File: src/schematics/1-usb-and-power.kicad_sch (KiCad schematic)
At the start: 49 parts, among them Q101 NX6008NBKW, U101 MP5016HGQH, U102 BQ24392RSER, U103 FUSB302BMPX, U104 TPS628512DRLR

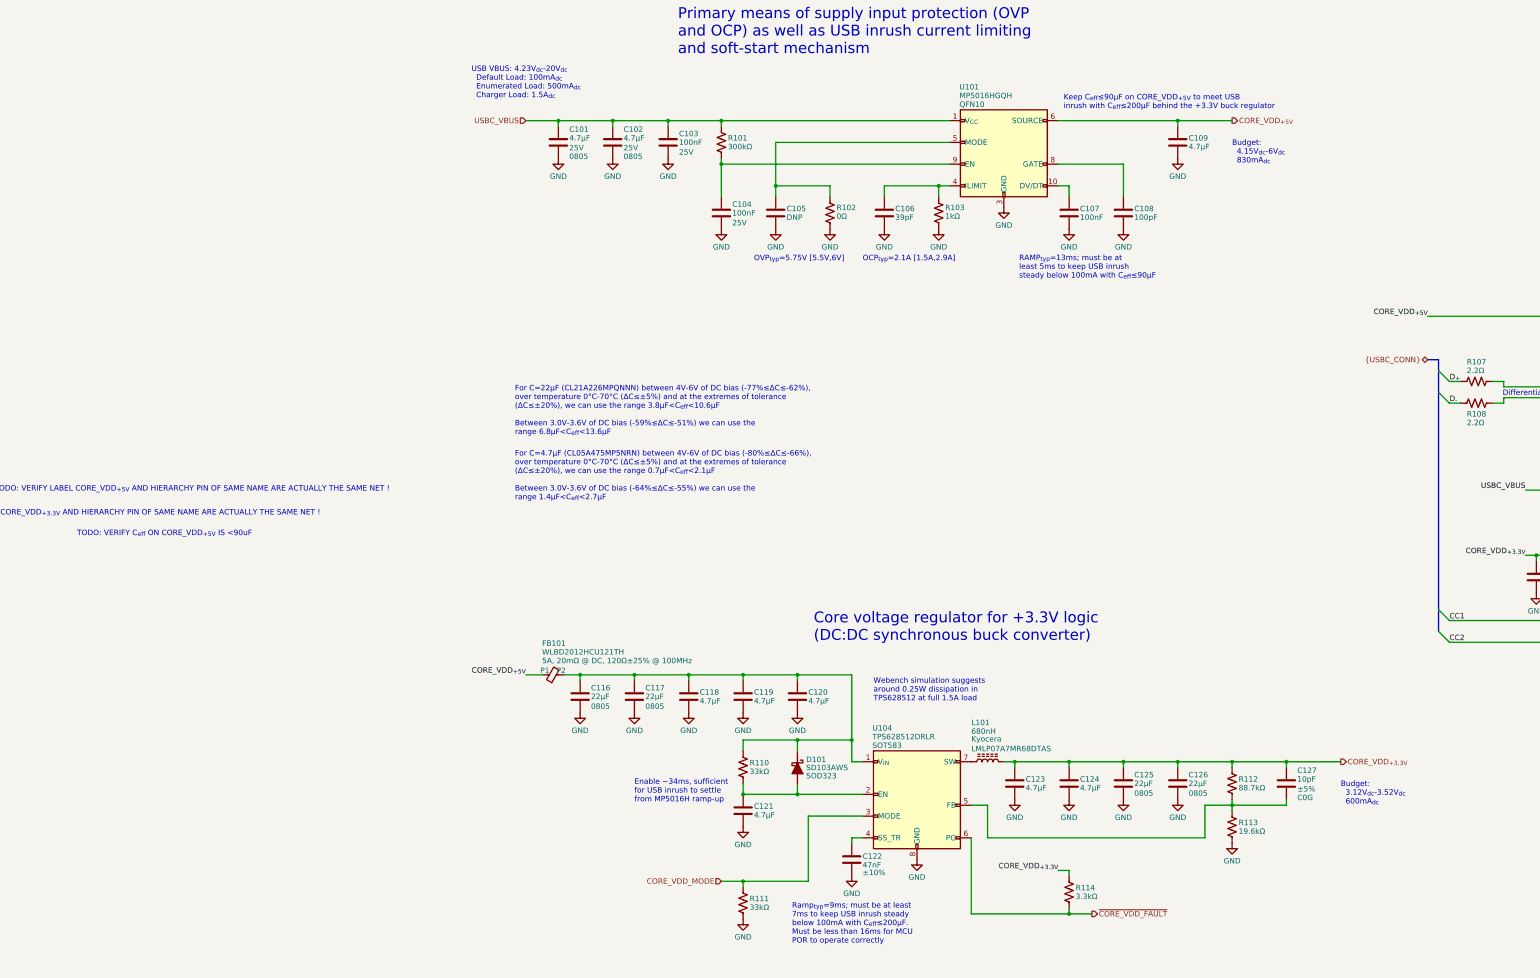
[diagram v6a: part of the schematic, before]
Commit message: Various tidy-ups and checks, mainly around the bypass capacitors.  Added a load of test points.
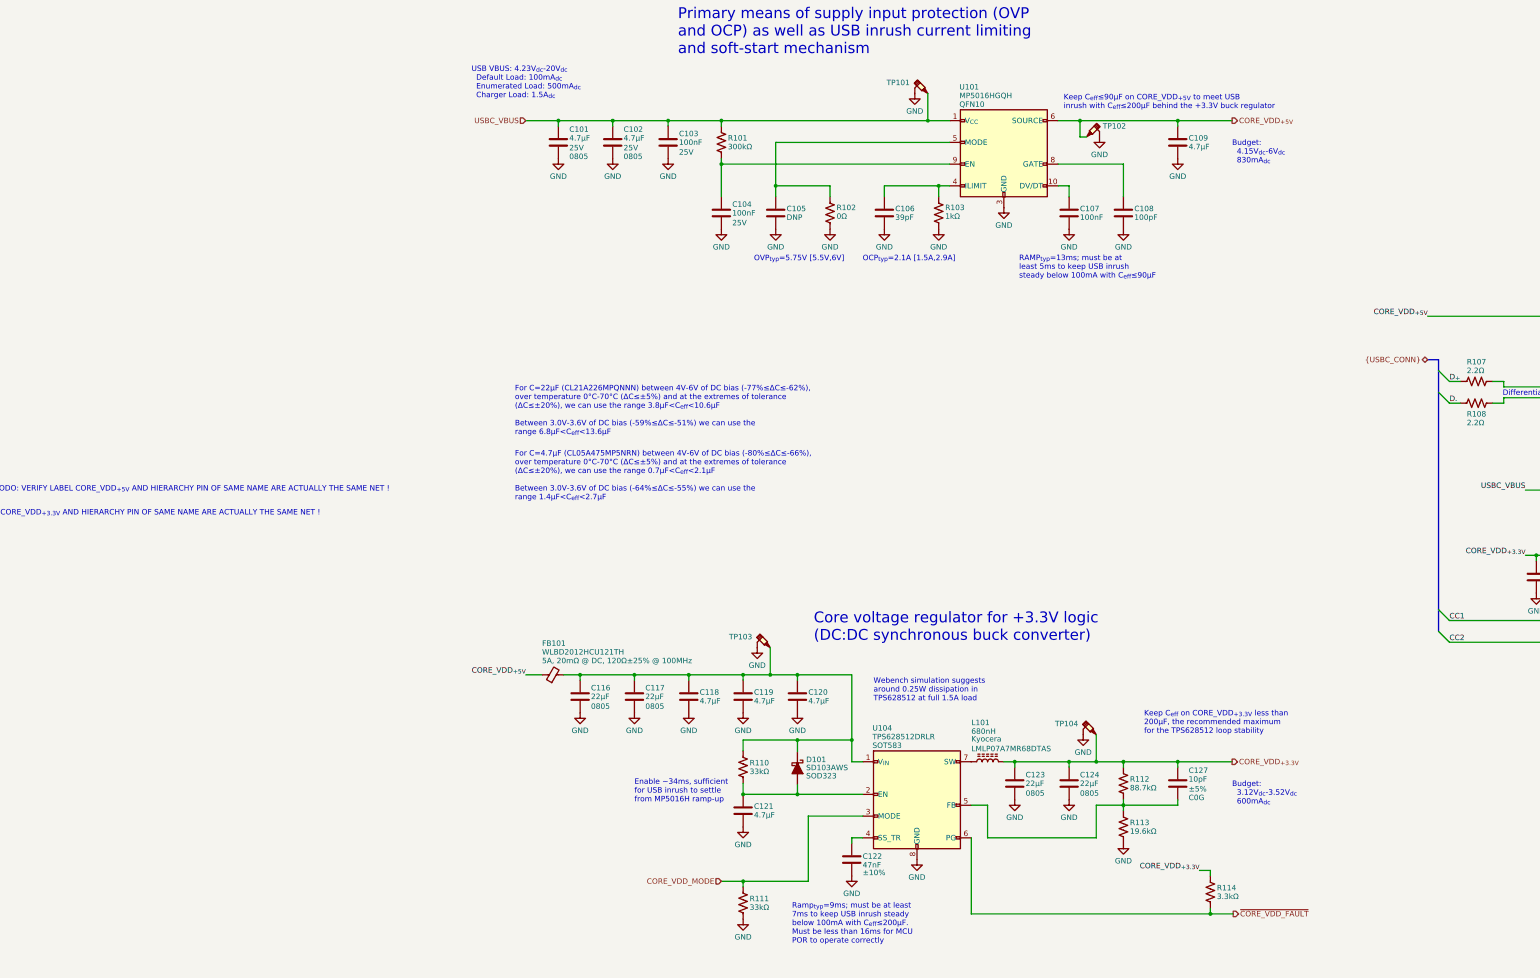
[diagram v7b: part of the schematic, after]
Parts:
- removed C123, C124: 4.7μF, restall-generic-capacitors:unpolarised-nominal-0402-1005, symbol restall-generic-capacitors:capacitor-unpolarised
- added TP101, TP102, TP103, TP104: ~, restall-generic-test:testpoint-SP3050A-with-short-gnd, symbol restall-generic-test:testpoint-probe-with-gnd
- renumbered C125 to C123, C126 to C124
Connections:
- net CORE_VDD_{+3.3V}: now also TP104.1
- net CORE_VDD_{+5V}: now also TP102.1
- net GND: now also TP101.2 (GND), TP102.2 (GND), TP103.2 (GND), TP104.2 (GND)
- net USBC_VBUS: now also TP101.1
- net at C116.1, C117.1, C118.1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: now also TP103.1
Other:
- note added: "Keep C_{eff} on CORE_VDD_{+3.3V} less than 200μF, the recommended maximum for the TPS628512 loop stability"
- note removed: "TODO: VERIFY C_{eff} ON CORE_VDD_{+5V} IS <90uF"
- moved on the sheet: C123, C124, C127, R112, R113, R114

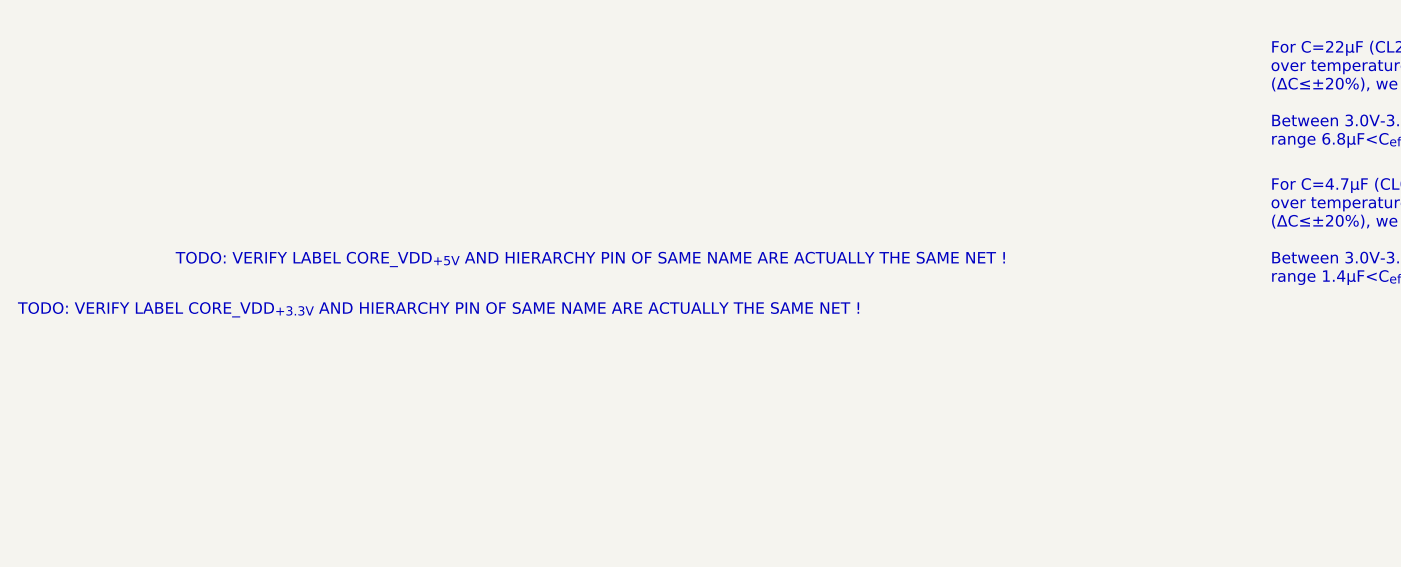
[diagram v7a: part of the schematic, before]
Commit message: Finalised various components and footprints.  Various tidy-ups.
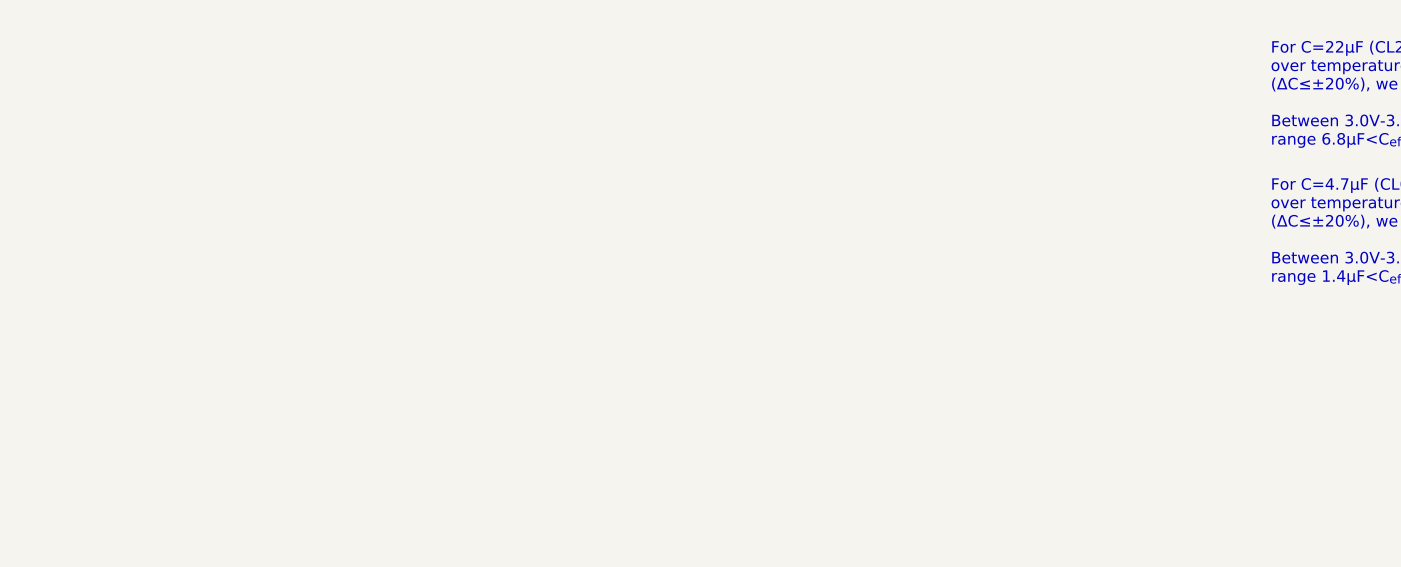
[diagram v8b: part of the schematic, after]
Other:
- note removed: "TODO: VERIFY LABEL CORE_VDD_{+3.3V} AND HIERARCHY PIN OF SAME NAME ARE ACTUALLY THE SAME NET !"
- note removed: "TODO: VERIFY LABEL CORE_VDD_{+5V} AND HIERARCHY PIN OF SAME NAME ARE ACTUALLY THE SAME NET !"
- title: (none) -> MSF Owl Clock - USB and Core Power Module
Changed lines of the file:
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@@
   (paper "A3")
   (title_block
+    (title "MSF Owl Clock - USB and Core Power Module")
     (rev "0.1")
     (company "Pete Restall <pete@restall.net>")
@@
     (effects (font (size 1.27 1.27)) (justify left bottom))
   )
-  (text "TODO: VERIFY LABEL CORE_VDD_{+5V} AND HIERARCHY PIN OF SAME NAME ARE ACTUALLY THE SAME NET !"
-    (at -96.266 150.368 0)
-    (effects (font (size 1.27 1.27)) (justify left bottom))
-  )
   (text "RAMP_{typ}=13ms; must be at\nleast 5ms to keep USB inrush\nsteady below 100mA with C_{eff}≤90μF"
     (at 143.256 100.584 0)
@@
     (effects (font (size 2.54 2.54)) (justify left bottom))
   )
-  (text "TODO: VERIFY LABEL CORE_VDD_{+3.3V} AND HIERARCHY PIN OF SAME NAME ARE ACTUALLY THE SAME NET !"
-    (at -113.792 155.956 0)
-    (effects (font (size 1.27 1.27)) (justify left bottom))
-  )
   (text "For C=4.7μF (CL05A475MP5NRN) between 4V-6V of DC bias (-80%≤ΔC≤-66%),\nover temperature 0°C-70°C (ΔC≤±5%) and at the extremes of tolerance\n(ΔC≤±20%), we can use the range 0.7μF<C_{eff}<2.1μF\n\nBetween 3.0V-3.6V of DC bias (-64%≤ΔC≤-55%) we can use the\nrange 1.4μF<C_{eff}<2.7μF"
